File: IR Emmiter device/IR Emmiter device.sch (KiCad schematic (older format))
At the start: 54 parts, among them J1 USB_C_Receptacle_USB2.0, J2 ICSP Header, J3 AudioJack3_Ground_Switch, J4 AudioJack3_Ground_Switch, J5 AudioJack3_Ground_Switch, J6 External Power, J7 TOP LED CONNECTION, J8 Conn_01x02_Female, Q1 FDS6890A, Q2 FDS6890A, Q3 FDS6890A, Q4 FDS6890A, SW1 SW_Push, SW2 SW_Push, U1 LM7805_TO220, U2 ATmega328-PU, U3 CH330N, Y1 8 MHz

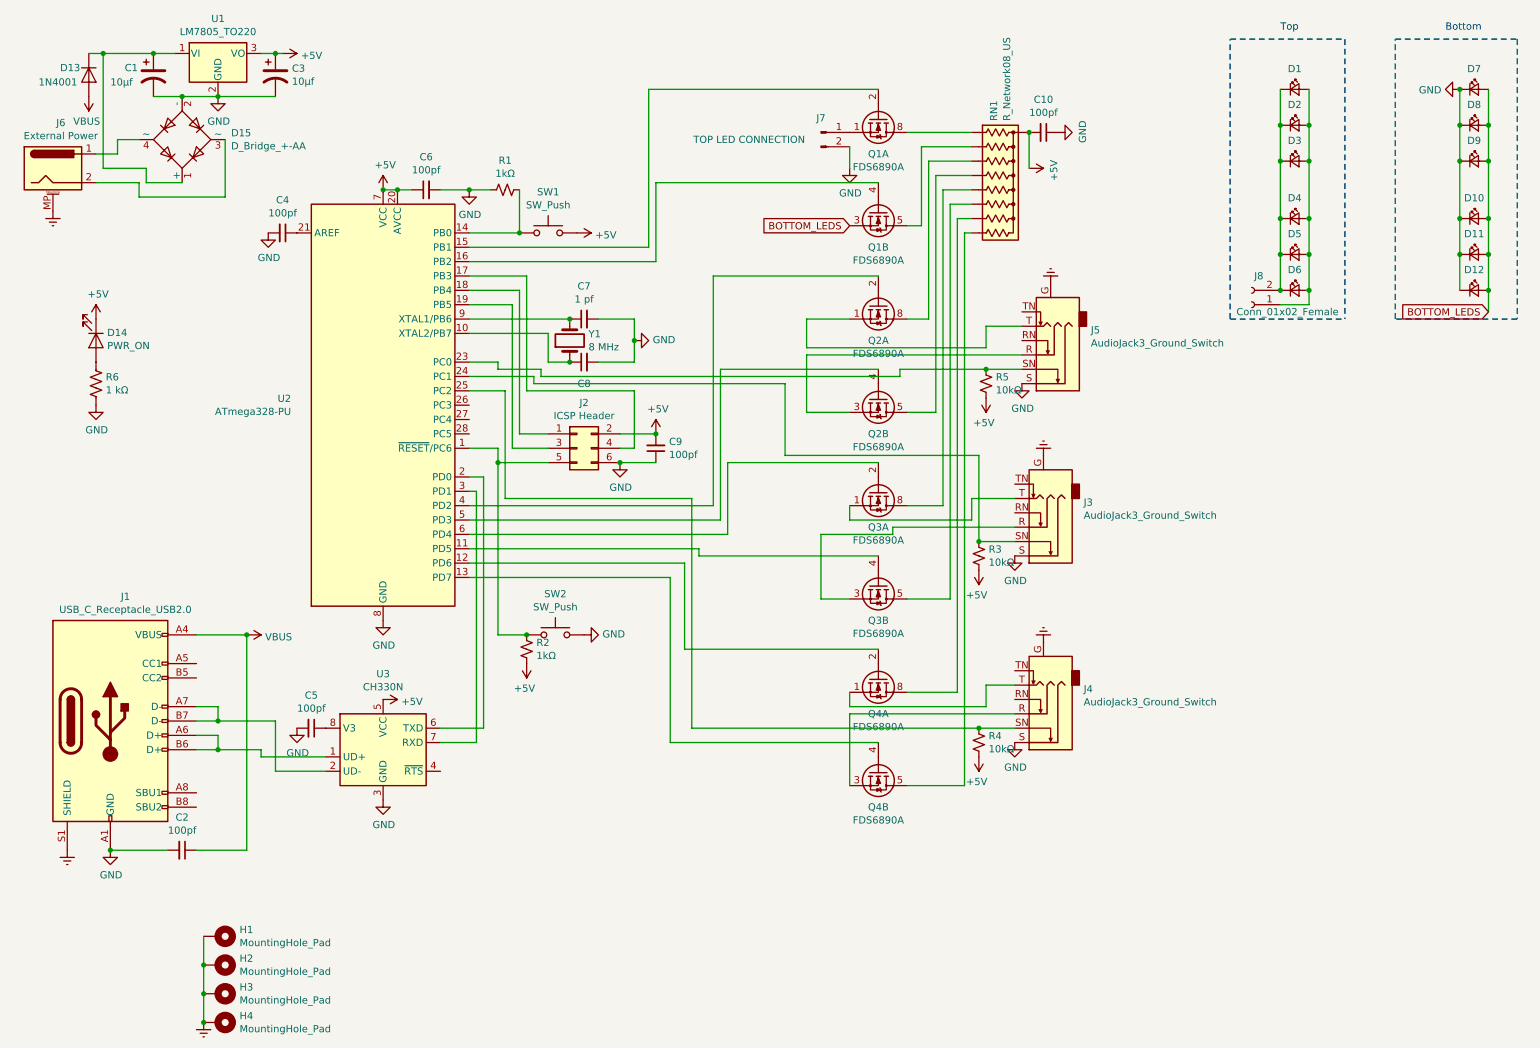
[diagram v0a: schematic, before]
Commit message: Minor changes to schematic, swapped out parts on PCB layout to aid in case design and added footprints for the expansions
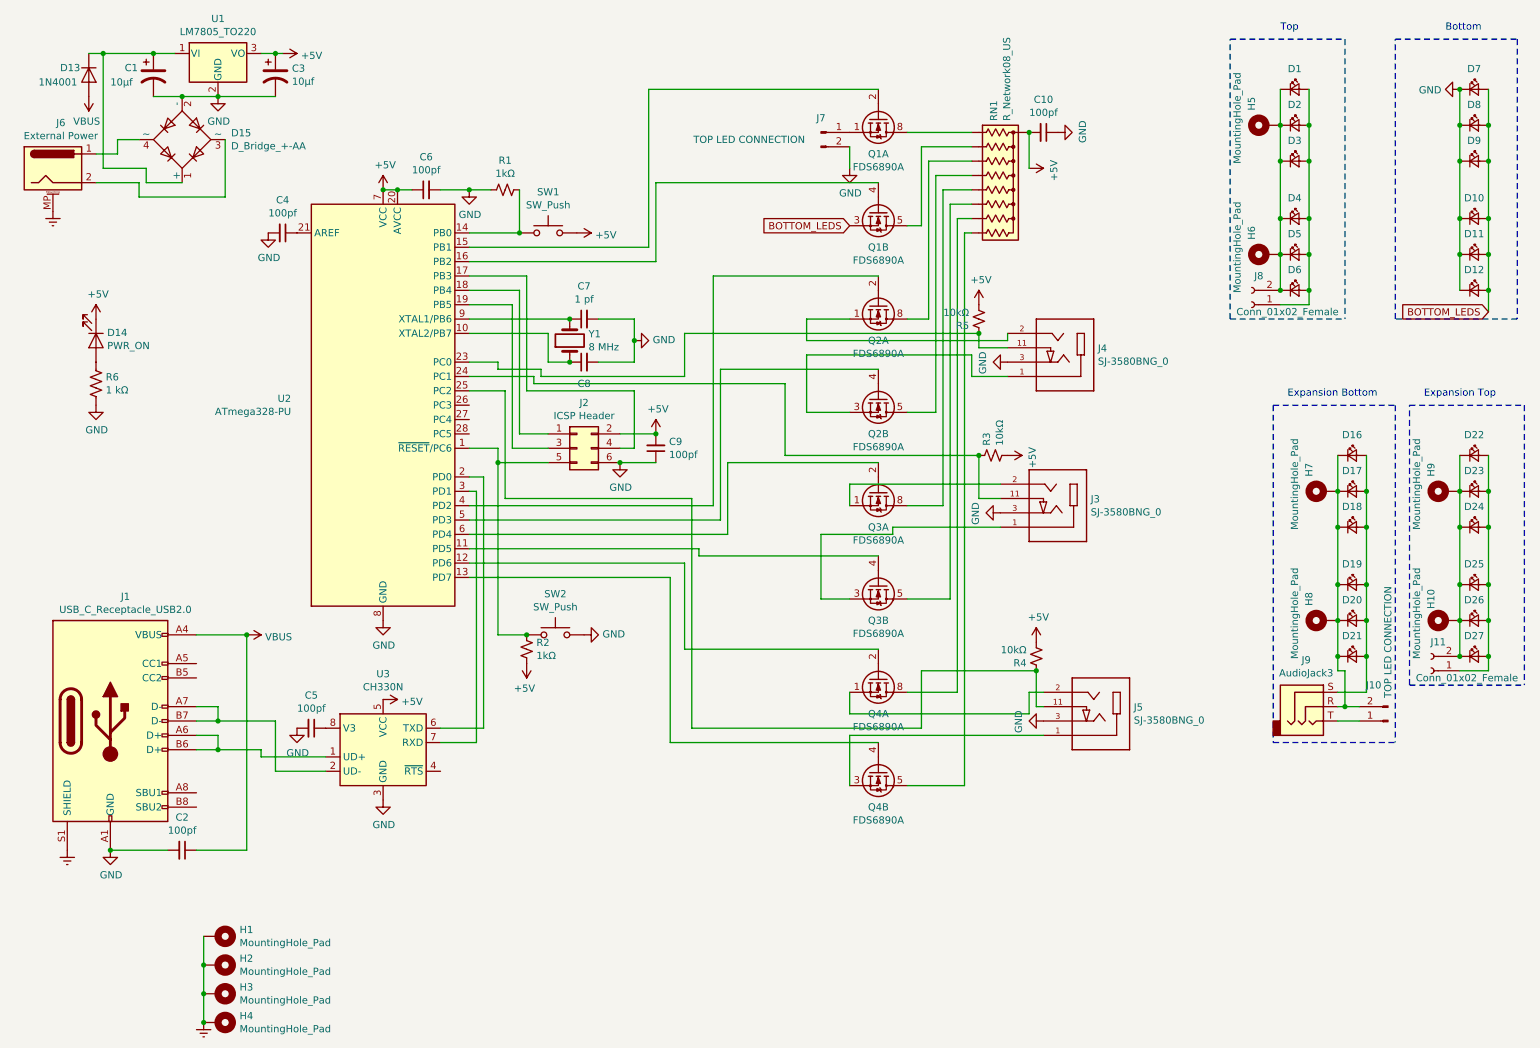
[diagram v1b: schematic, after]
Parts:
- removed J3, J4, J5: AudioJack3_Ground_Switch, Connector_Audio:Jack_3.5mm_Neutrik_NMJ6HCD2_Horizontal, symbol Connector:AudioJack3_Ground_Switch
- added D16, D17, D18, D19, D20, D21, D22, D23, D24, D25, D26, D27: LED_Small, LED_THT:LED_D5.0mm_Horizontal_O1.27mm_Z3.0mm_Clear, symbol Device:LED_Small
- added H10, H5, H6, H7, H8, H9: MountingHole_Pad, MountingHole:MountingHole_2.5mm_Pad_Via, symbol Mechanical:MountingHole_Pad
- added J10: TOP LED CONNECTION, Connector_PinHeader_2.54mm:PinHeader_1x02_P2.54mm_Vertical, symbol Connector:Conn_01x02_Male
- added J11: Conn_01x02_Female, Connector_PinSocket_2.54mm:PinSocket_1x02_P2.54mm_Vertical, symbol Connector:Conn_01x02_Female
- added J3, J4, J5: SJ-3580BNG_0, Connector_Audio:SJ-3580BNG, symbol SJ-3580BNG:SJ-3580BNG_0
- added J9: AudioJack3, Connector_Audio:Jack_3.5mm_CUI_SJ1-3533NG_Horizontal, symbol Connector:AudioJack3
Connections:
- net GND: now also J3.3, J4.3, J5.3
- net at R5.2, U2.23 (PC0): now also J4.11
- net at R3.2, U2.24 (PC1): now also J3.11
- net at R4.2, U2.25 (PC2): now also J5.11
- net at D1.1 (K), D2.1 (K), D3.1 (K)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: now also H5.1, H6.1
- net at Q2.3 (S2): now also J4.1
- net at Q2.1 (S1): now also J4.2
- net at Q3.3 (S2): now also J3.1
- net at Q3.1 (S1): now also J3.2
- net at Q4.3 (S2): now also J5.1
- net at Q4.1 (S1): now also J5.2
- new net: D22.1 (K), D23.1 (K), D24.1 (K), D25.1 (K), D26.1 (K), D27.1 (K), H10.1, H9.1, J11.2 (Pin_2)
- new net: D22.2 (A), D23.2 (A), D24.2 (A), D25.2 (A), D26.2 (A), D27.2 (A), J11.1 (Pin_1)
- new net: D16.1 (K), D17.1 (K), D18.1 (K), D19.1 (K), D20.1 (K), D21.1 (K), H7.1, H8.1, J10.2 (Pin_2), J9.R
- new net: D16.2 (A), D17.2 (A), D18.2 (A), D19.2 (A), D20.2 (A), D21.2 (A), J9.S
- new net: J10.1 (Pin_1), J9.T
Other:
- note added: "Expansion Bottom\n"
- note added: "Expansion Top"
- moved on the sheet: R5

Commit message: Completed basic shape of case for main unit, finished layout of PCB for improved sensor bar
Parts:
- added LOGO1: Logo_Open_Hardware_Large, Symbol:OSHW-Logo_5.7x6mm_SilkScreen, symbol Graphic:Logo_Open_Hardware_Large
- J1: footprint Connector_USB:USB_C_Receptacle_Amphenol_12401548E4-2A -> Connector_USB:USB4085-GF-A_REVA
- J3, J4, J5: symbol SJ-3580BNG:SJ-3580BNG_0 -> IR-Emmiter-device-rescue:SJ-3580BNG_0-SJ-3580BNG
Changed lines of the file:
@@
 F 0 "J1" H 1205 6367 50  0000 C CNN
 F 1 "USB_C_Receptacle_USB2.0" H 1205 6276 50  0000 C CNN
-F 2 "Connector_USB:USB_C_Receptacle_Amphenol_12401548E4-2A" H 1250 5500 50  0001 C CNN
+F 2 "Connector_USB:USB4085-GF-A_REVA" H 1250 5500 50  0001 C CNN
 F 3 "https://www.usb.org/sites/default/files/documents/usb_type-c.zip" H 1250 5500 50  0001 C CNN
 	1    1100 5500
@@
 	5100 3100 4100 3100
 $Comp
-L SJ-3580BNG:SJ-3580BNG_0 J4
+L IR-Emmiter-device-rescue:SJ-3580BNG_0-SJ-3580BNG J4
 U 1 1 5DD27667
 P 7700 2900
@@
 	7350 2850 5950 2850
 $Comp
-L SJ-3580BNG:SJ-3580BNG_0 J3
+L IR-Emmiter-device-rescue:SJ-3580BNG_0-SJ-3580BNG J3
 U 1 1 5DDA2628
 P 7650 3950
@@
 	6250 3850 6250 4000
 $Comp
-L SJ-3580BNG:SJ-3580BNG_0 J5
+L IR-Emmiter-device-rescue:SJ-3580BNG_0-SJ-3580BNG J5
 U 1 1 5DE2529E
 P 7950 5400
@@
 	9700 5400 9800 5400
 Connection ~ 9650 5050
+$Comp
+L Graphic:Logo_Open_Hardware_Large LOGO1
+U 1 1 5DB23FB7
+P 1000 7350
+F 0 "LOGO1" H 1000 7850 50  0001 C CNN
+F 1 "Logo_Open_Hardware_Large" H 1000 6950 50  0001 C CNN
+F 2 "Symbol:OSHW-Logo_5.7x6mm_SilkScreen" H 1000 7350 50  0001 C CNN
+F 3 "~" H 1000 7350 50  0001 C CNN
+	1    1000 7350
+	1    0    0    -1
+$EndComp
 $EndSCHEMATC
